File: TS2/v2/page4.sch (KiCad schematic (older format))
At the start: 5 parts

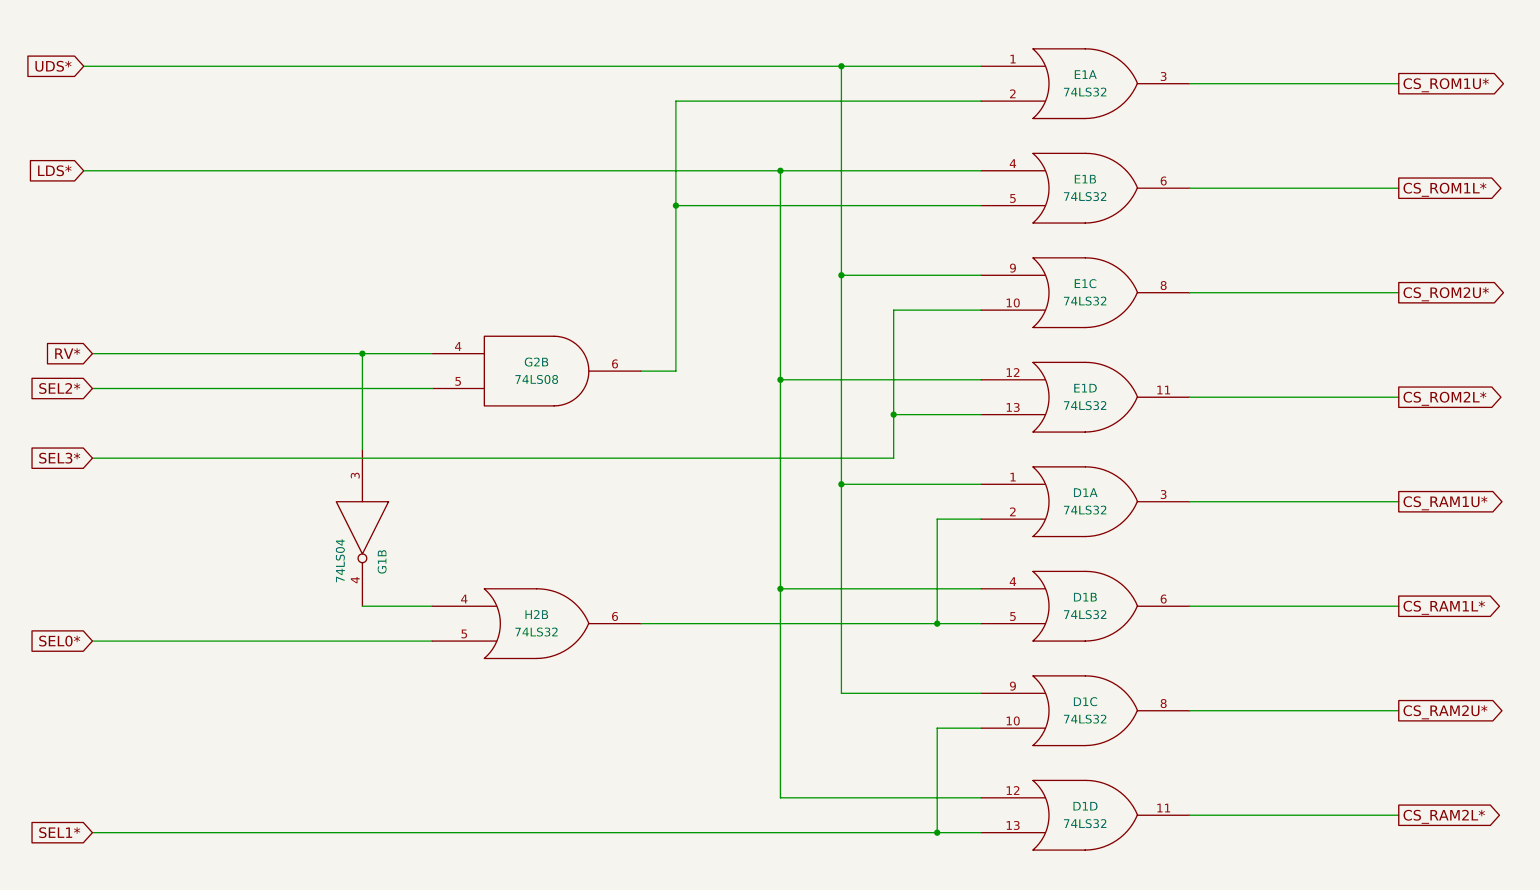
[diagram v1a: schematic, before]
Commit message: more fixup of deleted pages.
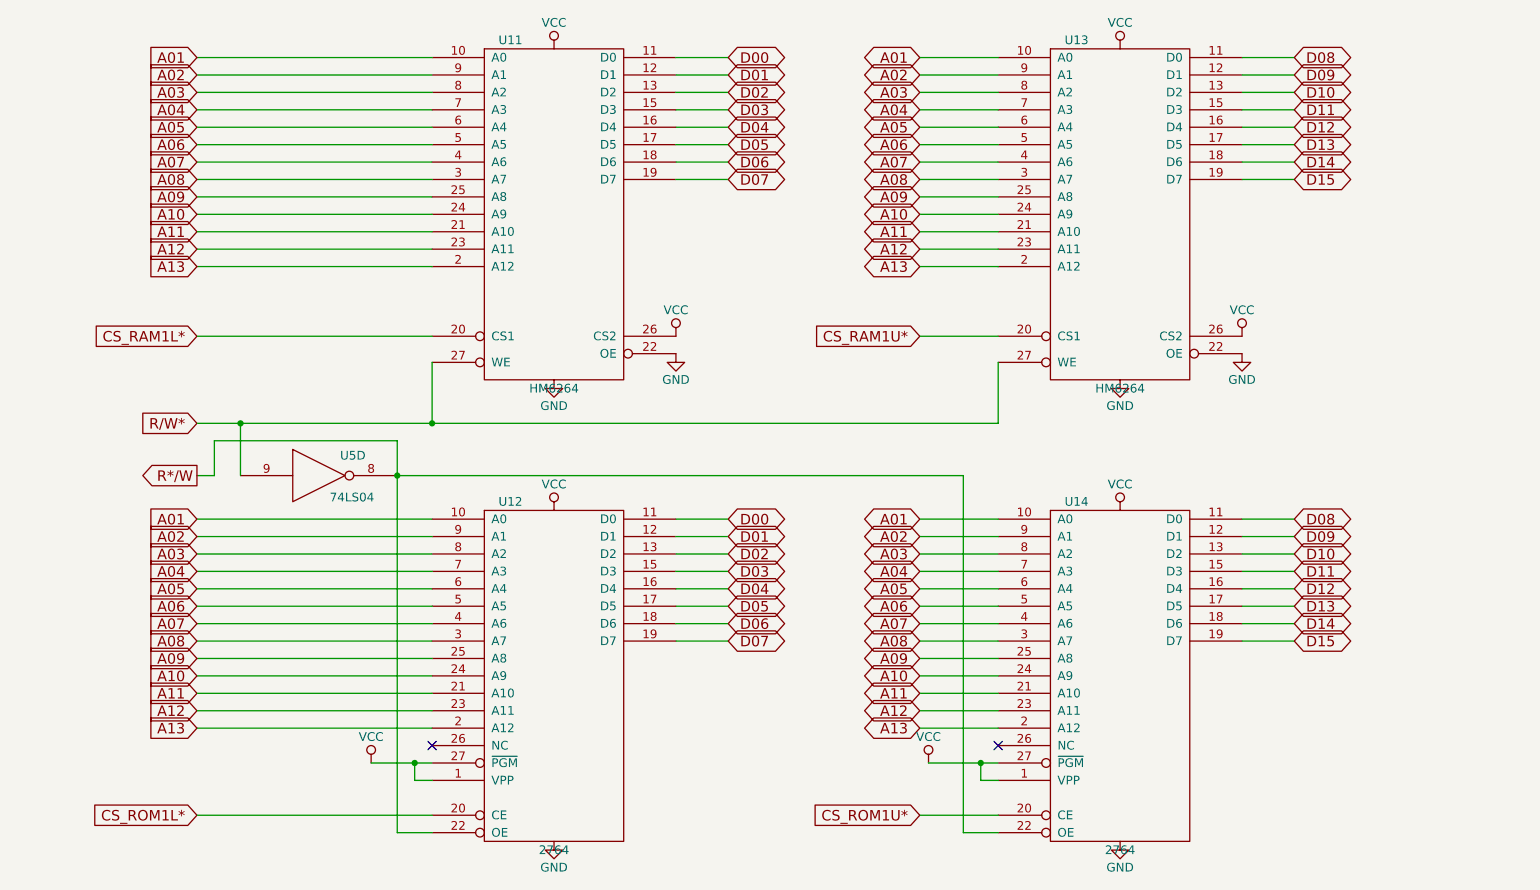
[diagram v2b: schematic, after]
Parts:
- removed D1, E1, H2: 74LS32, symbol 74LS32
- removed G1: 74LS04, symbol 74LS04
- removed G2: 74LS08, symbol 74LS08
- added U11, U13: HM6264, symbol HM6264
- added U12, U14: 2764, symbol 2764
- added U5: 74LS04, symbol 74LS04
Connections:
- net CS_RAM1L*: now also U11.20 (CS1)
- net CS_RAM1U*: now also U13.20 (CS1)
- net CS_ROM1L*: now also U12.20 (CE)
- net CS_ROM1U*: now also U14.20 (CE)
- net GND: now also U11.14 (GND), U11.22 (OE), U12.14 (GND), U13.14 (GND), U13.22 (OE), U14.14 (GND), U5.7 (GND)
- net VCC: now also U11.26 (CS2), U11.28 (VCC), U12.1 (VPP), U12.27 (~PGM), U12.28 (VCC), U13.26 (CS2), U13.28 (VCC), U14.1 (VPP), U14.27 (~PGM), U14.28 (VCC), U5.14 (VCC)
- new net A01: U11.10 (A0), U12.10 (A0), U13.10 (A0), U14.10 (A0)
- new net A02: U11.9 (A1), U12.9 (A1), U13.9 (A1), U14.9 (A1)
- new net A03: U11.8 (A2), U12.8 (A2), U13.8 (A2), U14.8 (A2)
- new net A04: U11.7 (A3), U12.7 (A3), U13.7 (A3), U14.7 (A3)
- new net A05: U11.6 (A4), U12.6 (A4), U13.6 (A4), U14.6 (A4)
- new net A06: U11.5 (A5), U12.5 (A5), U13.5 (A5), U14.5 (A5)
- new net A07: U11.4 (A6), U12.4 (A6), U13.4 (A6), U14.4 (A6)
- new net A08: U11.3 (A7), U12.3 (A7), U13.3 (A7), U14.3 (A7)
- new net A09: U11.25 (A8), U12.25 (A8), U13.25 (A8), U14.25 (A8)
- new net A10: U11.24 (A9), U12.24 (A9), U13.24 (A9), U14.24 (A9)
- new net A11: U11.21 (A10), U12.21 (A10), U13.21 (A10), U14.21 (A10)
- new net A12: U11.23 (A11), U12.23 (A11), U13.23 (A11), U14.23 (A11)
- new net A13: U11.2 (A12), U12.2 (A12), U13.2 (A12), U14.2 (A12)
- new net D00: U11.11 (D0), U12.11 (D0)
- new net D01: U11.12 (D1), U12.12 (D1)
- new net D02: U11.13 (D2), U12.13 (D2)
- new net D03: U11.15 (D3), U12.15 (D3)
- new net D04: U11.16 (D4), U12.16 (D4)
- new net D05: U11.17 (D5), U12.17 (D5)
- new net D06: U11.18 (D6), U12.18 (D6)
- new net D07: U11.19 (D7), U12.19 (D7)
- new net D08: U13.11 (D0), U14.11 (D0)
- new net D09: U13.12 (D1), U14.12 (D1)
- new net D10: U13.13 (D2), U14.13 (D2)
- new net D11: U13.15 (D3), U14.15 (D3)
- new net D12: U13.16 (D4), U14.16 (D4)
- new net D13: U13.17 (D5), U14.17 (D5)
- new net D14: U13.18 (D6), U14.18 (D6)
- new net D15: U13.19 (D7), U14.19 (D7)
- new net R*/W: U12.22 (OE), U14.22 (OE), U5.8
- new net R/W*: U11.27 (WE), U13.27 (WE), U5.9
- no-connect marks 0 -> 2
